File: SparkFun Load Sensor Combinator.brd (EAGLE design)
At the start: 27.9 x 30.5 mm, 13 parts

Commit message: Added DS18S20 connection.
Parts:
- added JP7: (no value), SparkFun-Connectors:1X03
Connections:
- new net 5V: JP6.3, JP7.3
- new net GND: JP6.1, JP7.1
- new net TEMP_DAT: JP6.2, JP7.2
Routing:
- net 5V: track 0.00 -> 15.3 mm
- net TEMP_DAT: track 0.00 -> 10.6 mm
- net GND: track 0.00 -> 10.4 mm
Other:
- board text added: "5V"
- board text added: "DAT"
- board text added: "DS18S20"
- board text added: "GND"

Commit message: Correcting name to DS18B20
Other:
- board text added: "DS18B20"
- board text removed: "DS18S20"
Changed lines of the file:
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@@
 <text x="25.273" y="22.225" size="1.27" layer="21" font="vector" ratio="15" rot="R180">DAT</text>
 <text x="25.273" y="19.685" size="1.27" layer="21" font="vector" ratio="15" rot="R180">5V</text>
-<text x="25.146" y="25.781" size="1.27" layer="22" font="vector" ratio="15" rot="MR270">DS18S20</text>
+<text x="25.146" y="25.781" size="1.27" layer="22" font="vector" ratio="15" rot="MR270">DS18B20</text>
 </plain>
 <attributes>

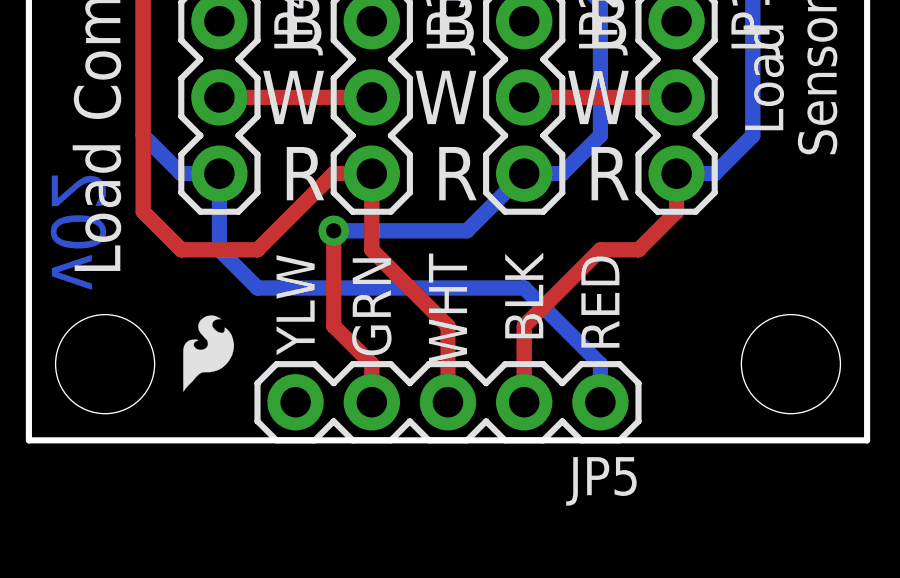
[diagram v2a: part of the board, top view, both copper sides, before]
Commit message: Bumped silk and rev 02
Fixed issue #1
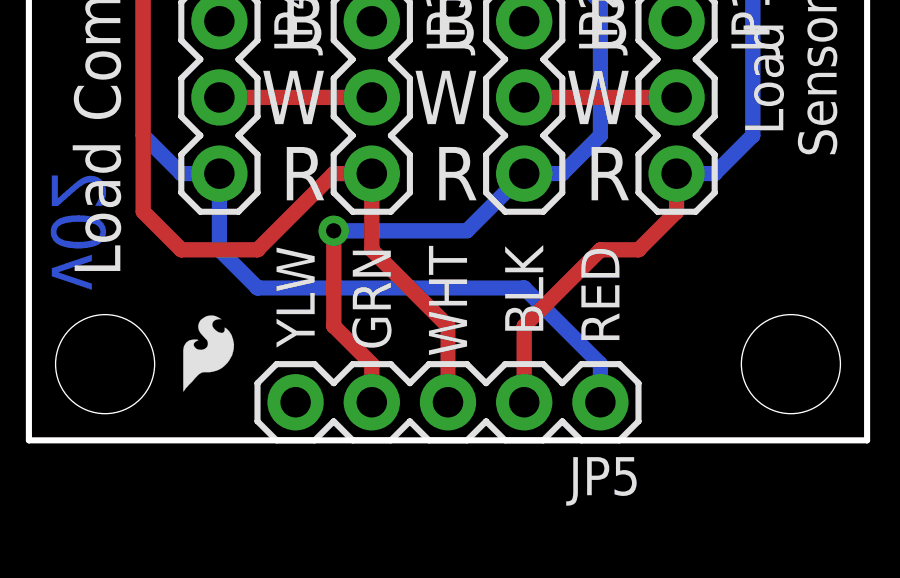
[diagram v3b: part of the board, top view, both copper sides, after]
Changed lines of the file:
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@@
 <?xml version="1.0" encoding="utf-8"?>
 <!DOCTYPE eagle SYSTEM "eagle.dtd">
-<eagle version="7.1.0">
+<eagle version="7.2.0">
 <drawing>
 <settings>
@@
 <wire x1="0" y1="30.48" x2="27.94" y2="30.48" width="0.2032" layer="20"/>
 <wire x1="27.94" y1="30.48" x2="27.94" y2="0" width="0.2032" layer="20"/>
-<text x="10.795" y="6.223" size="1.27" layer="21" font="vector" ratio="15" rot="R270">GRN</text>
+<text x="10.795" y="6.477" size="1.27" layer="21" font="vector" ratio="15" rot="R270">GRN</text>
 <text x="23.622" y="15.748" size="1.524" layer="22" font="vector" ratio="15" rot="MR0">Load Combinator</text>
-<text x="15.875" y="6.223" size="1.27" layer="21" font="vector" ratio="15" rot="R270">BLK</text>
-<text x="13.335" y="6.223" size="1.27" layer="21" font="vector" ratio="15" rot="R270">WHT</text>
-<text x="18.415" y="6.223" size="1.27" layer="21" font="vector" ratio="15" rot="R270">RED</text>
-<text x="10.795" y="2.54" size="1.27" layer="22" font="vector" ratio="15" rot="MR90">A+</text>
-<text x="13.335" y="2.54" size="1.27" layer="22" font="vector" ratio="15" rot="MR90">A-</text>
-<text x="15.875" y="2.54" size="1.27" layer="22" font="vector" ratio="15" rot="MR90">E-</text>
-<text x="18.415" y="2.54" size="1.27" layer="22" font="vector" ratio="15" rot="MR90">E+</text>
+<text x="15.875" y="6.477" size="1.27" layer="21" font="vector" ratio="15" rot="R270">BLK</text>
+<text x="13.335" y="6.477" size="1.27" layer="21" font="vector" ratio="15" rot="R270">WHT</text>
+<text x="18.415" y="6.477" size="1.27" layer="21" font="vector" ratio="15" rot="R270">RED</text>
+<text x="10.795" y="2.794" size="1.27" layer="22" font="vector" ratio="15" rot="MR90">A+</text>
+<text x="13.335" y="2.794" size="1.27" layer="22" font="vector" ratio="15" rot="MR90">A-</text>
+<text x="15.875" y="2.794" size="1.27" layer="22" font="vector" ratio="15" rot="MR90">E-</text>
+<text x="18.415" y="2.794" size="1.27" layer="22" font="vector" ratio="15" rot="MR90">E+</text>
 <text x="20.574" y="15.748" size="1.27" layer="21" font="vector" ratio="15">UL</text>
 <text x="15.494" y="15.748" size="1.27" layer="21" font="vector" ratio="15">UR</text>
@@
 <text x="20.066" y="9.779" size="1.778" layer="21" font="vector" ratio="15" rot="R180">R</text>
 <text x="0.762" y="4.953" size="1.778" layer="16" font="vector" ratio="15" rot="MR90">v02</text>
-<text x="8.255" y="6.223" size="1.27" layer="21" font="vector" ratio="15" rot="R270">YLW</text>
-<text x="8.255" y="2.54" size="1.27" layer="22" font="vector" ratio="15" rot="MR90">SLD</text>
+<text x="8.255" y="6.477" size="1.27" layer="21" font="vector" ratio="15" rot="R270">YLW</text>
+<text x="8.255" y="2.794" size="1.27" layer="22" font="vector" ratio="15" rot="MR90">SLD</text>
 <text x="0" y="49.53" size="1.778" layer="47" font="vector" ratio="15">Units are in inches</text>
 <text x="17.78" y="-11.43" size="1.778" layer="51" font="vector" ratio="15">N. Seidle</text>
@@
 <element name="JP4" library="SparkFun-Connectors" package="1X03" value="LR" x="6.35" y="13.97" rot="R270"/>
 <element name="FRAME1" library="SparkFun-Aesthetics" package="CREATIVE_COMMONS" value="" x="-12.7" y="-11.43">
-<attribute name="VERSION" value="v01" x="-12.7" y="-11.43" size="1.778" layer="27" font="vector" ratio="15" display="off"/>
+<attribute name="VERSION" value="v02" x="-12.7" y="-11.43" size="1.778" layer="27" font="vector" ratio="15" display="off"/>
 <attribute name="DESIGNER" value="N. Seidle" x="-12.7" y="-11.43" size="1.778" layer="27" font="vector" ratio="15" display="off"/>
 </element>

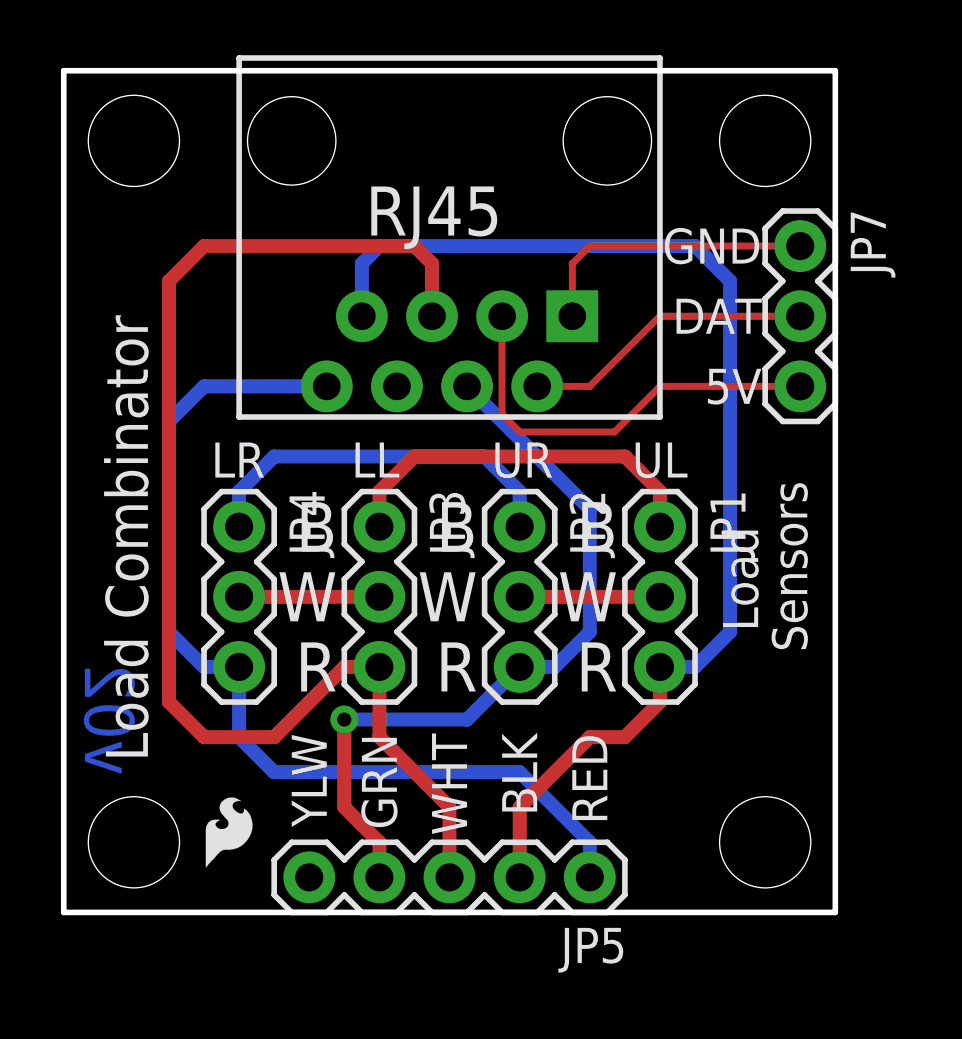
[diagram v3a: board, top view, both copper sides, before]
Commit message: Fixed a swap between A+ and A-
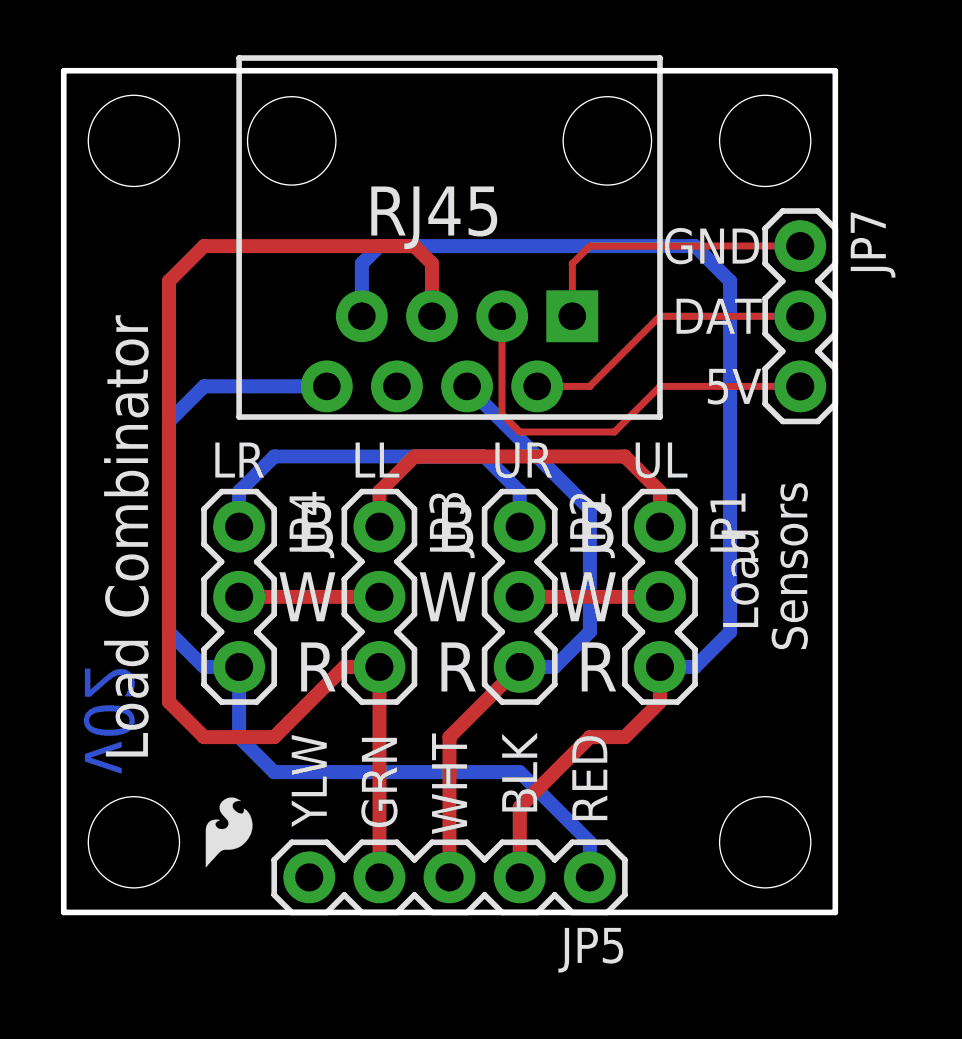
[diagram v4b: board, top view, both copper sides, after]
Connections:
- net A+: now also JP5.4; no longer JP5.3
- net A-: now also JP5.3; no longer JP5.4
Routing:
- net A-: track 27.2 -> 22.5 mm, vias 1 -> 0
- net A+: track 45.3 -> 44.3 mm
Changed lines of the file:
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@@
 <?xml version="1.0" encoding="utf-8"?>
 <!DOCTYPE eagle SYSTEM "eagle.dtd">
-<eagle version="7.2.0">
+<eagle version="7.1.0">
 <drawing>
 <settings>
@@
 <layer number="47" name="Measures" color="7" fill="1" visible="no" active="yes"/>
 <layer number="48" name="Document" color="7" fill="1" visible="no" active="yes"/>
-<layer number="49" name="Reference" color="7" fill="1" visible="yes" active="yes"/>
+<layer number="49" name="Reference" color="7" fill="1" visible="no" active="yes"/>
 <layer number="50" name="dxf" color="7" fill="1" visible="no" active="no"/>
 <layer number="51" name="tDocu" color="6" fill="1" visible="yes" active="yes"/>
@@
 <signal name="A+">
 <contactref element="JP3" pad="3"/>
-<contactref element="JP5" pad="3"/>
-<wire x1="11.43" y1="8.89" x2="11.43" y2="6.35" width="0.508" layer="1"/>
-<wire x1="11.43" y1="6.35" x2="13.97" y2="3.81" width="0.508" layer="1"/>
-<wire x1="13.97" y1="3.81" x2="13.97" y2="1.27" width="0.508" layer="1"/>
+<wire x1="11.43" y1="8.89" x2="11.43" y2="1.27" width="0.508" layer="1"/>
 <contactref element="JP6" pad="5"/>
 <wire x1="11.43" y1="8.89" x2="10.16" y2="8.89" width="0.508" layer="1"/>
@@
 <wire x1="13.335" y1="21.59" x2="13.335" y2="23.495" width="0.508" layer="1"/>
 <wire x1="13.335" y1="23.495" x2="12.7" y2="24.13" width="0.508" layer="1"/>
+<contactref element="JP5" pad="4"/>
 </signal>
 <signal name="A-">
 <contactref element="JP2" pad="3"/>
-<contactref element="JP5" pad="4"/>
-<wire x1="16.51" y1="8.89" x2="14.605" y2="6.985" width="0.508" layer="16"/>
-<wire x1="14.605" y1="6.985" x2="10.16" y2="6.985" width="0.508" layer="16"/>
-<via x="10.16" y="6.985" extent="1-16" drill="0.508"/>
-<wire x1="10.16" y1="6.985" x2="10.16" y2="3.81" width="0.508" layer="1"/>
-<wire x1="10.16" y1="3.81" x2="11.43" y2="2.54" width="0.508" layer="1"/>
-<wire x1="11.43" y1="2.54" x2="11.43" y2="1.27" width="0.508" layer="1"/>
 <wire x1="16.51" y1="8.89" x2="17.78" y2="8.89" width="0.508" layer="16"/>
 <wire x1="17.78" y1="8.89" x2="19.05" y2="10.16" width="0.508" layer="16"/>
@@
 <wire x1="14.605" y1="19.05" x2="19.05" y2="14.605" width="0.508" layer="16"/>
 <wire x1="19.05" y1="14.605" x2="19.05" y2="10.16" width="0.508" layer="16"/>
+<contactref element="JP5" pad="3"/>
+<wire x1="13.97" y1="1.27" x2="13.97" y2="6.35" width="0.508" layer="1"/>
+<wire x1="13.97" y1="6.35" x2="16.51" y2="8.89" width="0.508" layer="1"/>
 </signal>
 <signal name="E-">
